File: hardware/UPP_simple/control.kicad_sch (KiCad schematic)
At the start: 9 parts, among them U1 STM32G0C1KCTxN

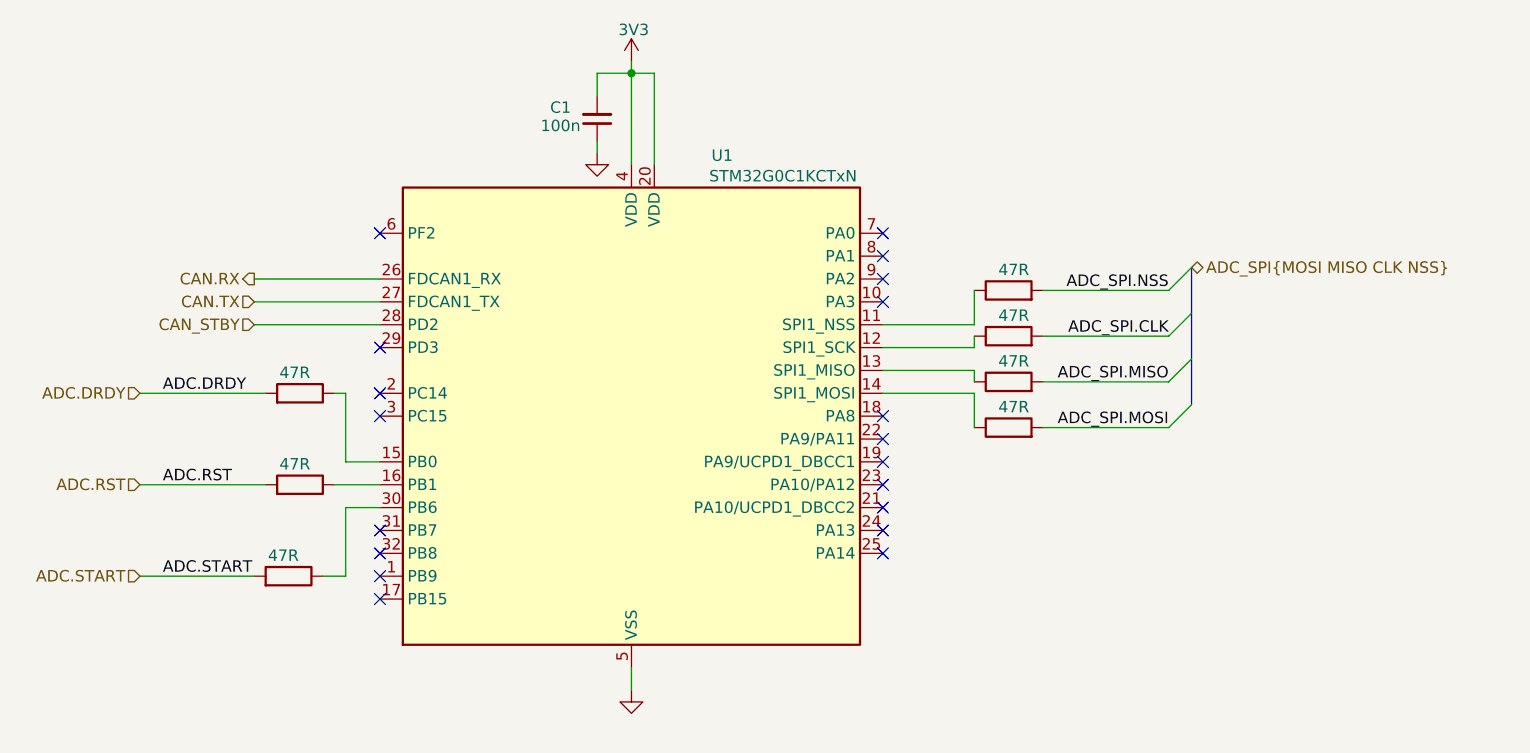
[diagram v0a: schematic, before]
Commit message: Changed Opamps cleared schematic
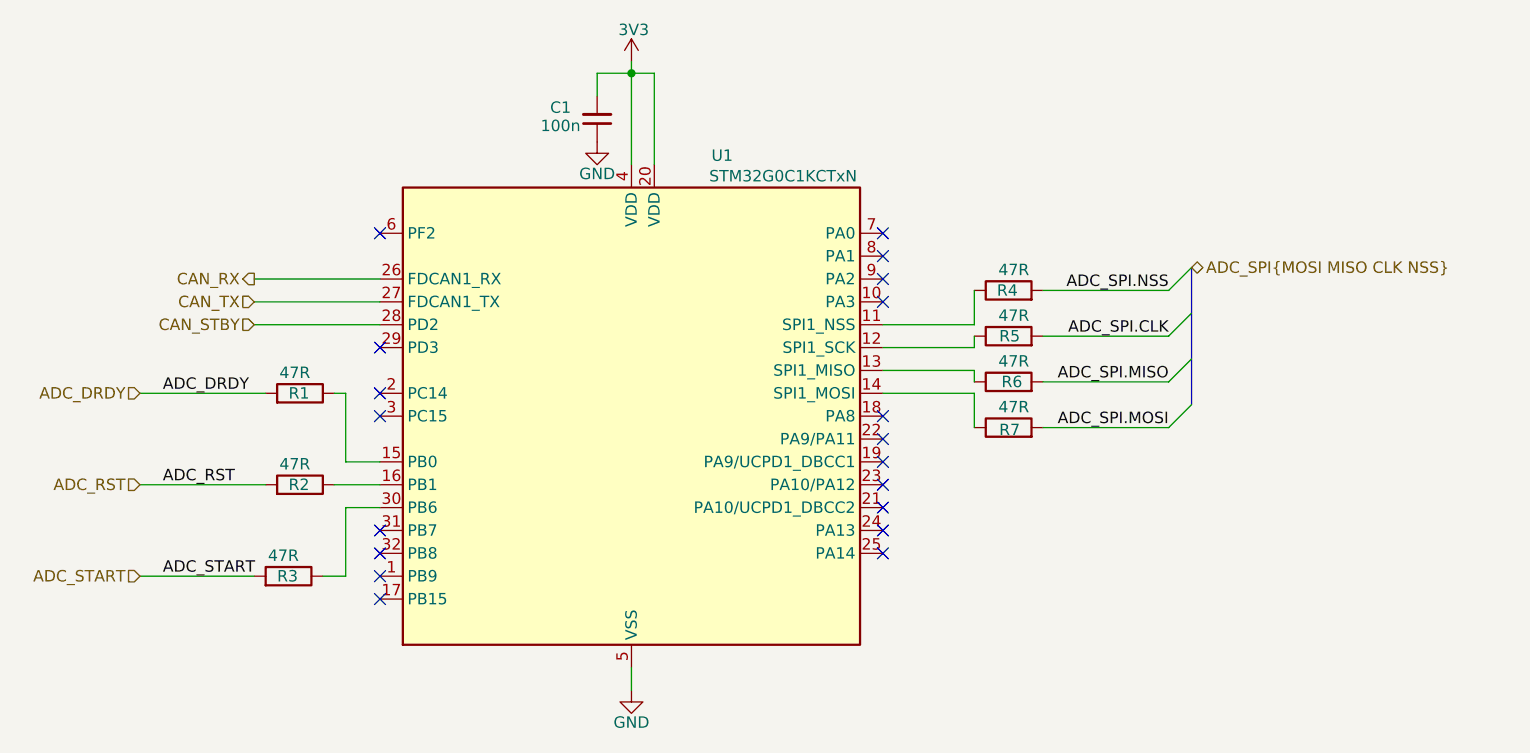
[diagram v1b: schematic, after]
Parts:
- renumbered R9 to R1, R15 to R2, R14 to R3, R13 to R4, R12 to R5, R11 to R6, R10 to R7
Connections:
- net ADC.DRDY renamed ADC_DRDY
- net ADC.RST renamed ADC_RST
- net ADC.START renamed ADC_START
- net CAN.RX renamed CAN_RX
- net CAN.TX renamed CAN_TX
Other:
- title: Universal use measuring PCB -> Universal Measurement Board
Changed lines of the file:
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@@
 	(paper "A4")
 	(title_block
-		(title "Universal use measuring PCB")
+		(title "Universal Measurement Board")
 		(company "Author: Kacper Pawlak")
 	)
@@
 		(pts
 			(xy 171.45 90.17) (xy 161.29 90.17)
-		)
-		(stroke
-			(width 0)
-			(type default)
-		)
-	)
-	(wire
-		(pts
-			(xy 129.54 62.23) (xy 129.54 63.5)
 		)
 		(stroke
@@
 		)
 	)
-	(label "ADC.RST"
+	(label "ADC_RST"
 		(at 81.28 100.33 0)
 		(effects
@@
 		)
 	)
-	(label "ADC.DRDY"
+	(label "ADC_DRDY"
 		(at 81.28 90.17 0)
 		(effects
@@
 		)
 	)
-	(label "ADC.START"
+	(label "ADC_START"
 		(at 81.28 110.49 0)
 		(effects
@@
 		)
 	)
-	(hierarchical_label "ADC.RST"
+	(hierarchical_label "ADC_RST"
 		(shape input)
 		(at 78.74 100.33 180)
@@
 		)
 	)
-	(hierarchical_label "CAN.TX"
+	(hierarchical_label "CAN_TX"
 		(shape input)
 		(at 91.44 80.01 180)
@@
 		)
 	)
-	(hierarchical_label "ADC.DRDY"
+	(hierarchical_label "ADC_DRDY"
 		(shape input)
 		(at 78.74 90.17 180)
@@
 		)
 	)
-	(hierarchical_label "CAN.RX"
+	(hierarchical_label "CAN_RX"
 		(shape output)
 		(at 91.44 77.47 180)
@@
 		)
 	)
-	(hierarchical_label "ADC.START"
+	(hierarchical_label "ADC_START"
 		(shape input)
 		(at 78.74 110.49 180)
@@
 		(on_board yes)
 		(dnp no)
-		(fields_autoplaced yes)
 		(property "Reference" "#PWR03"
 			(at 133.35 129.54 0)
@@
 		)
 		(property "Value" "GND"
-			(at 133.35 128.27 0)
-			(effects
-				(font
-					(size 1.27 1.27)
-				)
-				(hide yes)
+			(at 133.35 126.746 0)
+			(effects
+				(font
+					(size 1.27 1.27)
+				)
 			)
 		)
@@
 		(on_board yes)
 		(dnp no)
-		(property "Reference" "R14"
-			(at 96.5201 107.95 90)
-			(effects
-				(font
-					(size 1.27 1.27)
-				)
-				(justify left)
-				(hide yes)
+		(property "Reference" "R3"
+			(at 93.98 110.49 90)
+			(effects
+				(font
+					(size 1.27 1.27)
+				)
+				(justify left)
 			)
 		)
@@
 			(project "UPP_simple"
 				(path "/b652b05a-4e3d-4ad1-b032-18886abe7d45/e37d7555-464e-4542-8460-133370bc5076"
-					(reference "R14")
-					(unit 1)
-				)
-			)
-		)
-	)
-	(symbol
-		(lib_id "power:GND")
-		(at 129.54 63.5 0)
-		(unit 1)
-		(exclude_from_sim no)
-		(in_bom yes)
-		(on_board yes)
-		(dnp no)
-		(fields_autoplaced yes)
-		(property "Reference" "#PWR067"
-			(at 129.54 69.85 0)
-			(effects
-				(font
-					(size 1.27 1.27)
-				)
-				(hide yes)
-			)
-		)
-		(property "Value" "GND"
-			(at 129.54 68.58 0)
-			(effects
-				(font
-					(size 1.27 1.27)
-				)
-				(hide yes)
-			)
-		)
-		(property "Footprint" ""
-			(at 129.54 63.5 0)
-			(effects
-				(font
-					(size 1.27 1.27)
-				)
-				(hide yes)
-			)
-		)
-		(property "Datasheet" ""
-			(at 129.54 63.5 0)
-			(effects
-				(font
-					(size 1.27 1.27)
-				)
-				(hide yes)
-			)
-		)
-		(property "Description" "Power symbol creates a global label with name \"GND\" , ground"
-			(at 129.54 63.5 0)
-			(effects
-				(font
-					(size 1.27 1.27)
-				)
-				(hide yes)
-			)
-		)
-		(pin "1"
-		)
-		(instances
-			(project "UPP_simple"
-				(path "/b652b05a-4e3d-4ad1-b032-18886abe7d45/e37d7555-464e-4542-8460-133370bc5076"
-					(reference "#PWR067")
+					(reference "R3")
 					(unit 1)
 				)
@@
 		(on_board yes)
 		(dnp no)
-		(property "Reference" "R9"
-			(at 97.7901 87.63 90)
-			(effects
-				(font
-					(size 1.27 1.27)
-				)
-				(justify left)
-				(hide yes)
+		(property "Reference" "R1"
+			(at 95.25 90.17 90)
+			(effects
+				(font
+					(size 1.27 1.27)
+				)
+				(justify left)
 			)
 		)
@@
 			(project "UPP_simple"
 				(path "/b652b05a-4e3d-4ad1-b032-18886abe7d45/e37d7555-464e-4542-8460-133370bc5076"
-					(reference "R9")
+					(reference "R1")
 					(unit 1)
 				)
@@
 		(on_board yes)
 		(dnp no)
-		(property "Reference" "R15"
-			(at 97.7901 97.79 90)
-			(effects
-				(font
-					(size 1.27 1.27)
-				)
-				(justify left)
-				(hide yes)
+		(property "Reference" "R2"
+			(at 95.25 100.33 90)
+			(effects
+				(font
+					(size 1.27 1.27)
+				)
+				(justify left)
 			)
 		)
@@
 			(project "UPP_simple"
 				(path "/b652b05a-4e3d-4ad1-b032-18886abe7d45/e37d7555-464e-4542-8460-133370bc5076"
-					(reference "R15")
+					(reference "R2")
 					(unit 1)
 				)
@@
 		(on_board yes)
 		(dnp no)
-		(property "Reference" "R13"
-			(at 173.9899 76.2 90)
-			(effects
-				(font
-					(size 1.27 1.27)
-				)
-				(justify left)
-				(hide yes)
+		(property "Reference" "R4"
+			(at 176.276 78.74 90)
+			(effects
+				(font
+					(size 1.27 1.27)
+				)
+				(justify left)
 			)
 		)
@@
 			(project "UPP_simple"
 				(path "/b652b05a-4e3d-4ad1-b032-18886abe7d45/e37d7555-464e-4542-8460-133370bc5076"
-					(reference "R13")
+					(reference "R4")
 					(unit 1)
 				)
@@
 		(on_board yes)
 		(dnp no)
-		(property "Reference" "R11"
-			(at 173.9899 86.36 90)
-			(effects
-				(font
-					(size 1.27 1.27)
-				)
-				(justify left)
-				(hide yes)
+		(property "Reference" "R6"
+			(at 176.784 88.9 90)
+			(effects
+				(font
+					(size 1.27 1.27)
+				)
+				(justify left)
 			)
 		)
@@
 			(project "UPP_simple"
 				(path "/b652b05a-4e3d-4ad1-b032-18886abe7d45/e37d7555-464e-4542-8460-133370bc5076"
-					(reference "R11")
+					(reference "R6")
 					(unit 1)
 				)
@@
 	)
 	(symbol
+		(lib_id "power:GND")
+		(at 129.54 62.23 0)
+		(unit 1)
+		(exclude_from_sim no)
+		(in_bom yes)
+		(on_board yes)
+		(dnp no)
+		(property "Reference" "#PWR043"
+			(at 129.54 68.58 0)
+			(effects
+				(font
+					(size 1.27 1.27)
+				)
+				(hide yes)
+			)
+		)
+		(property "Value" "GND"
+			(at 129.54 65.786 0)
+			(effects
+				(font
+					(size 1.27 1.27)
+				)
+			)
+		)
+		(property "Footprint" ""
+			(at 129.54 62.23 0)
+			(effects
+				(font
+					(size 1.27 1.27)
+				)
+				(hide yes)
+			)
+		)
+		(property "Datasheet" ""
+			(at 129.54 62.23 0)
+			(effects
+				(font
+					(size 1.27 1.27)
+				)
+				(hide yes)
+			)
+		)
+		(property "Description" "Power symbol creates a global label with name \"GND\" , ground"
+			(at 129.54 62.23 0)
+			(effects
+				(font
+					(size 1.27 1.27)
+				)
+				(hide yes)
+			)
+		)
+		(pin "1"
+		)
+		(instances
+			(project "UMB"
+				(path "/b652b05a-4e3d-4ad1-b032-18886abe7d45/e37d7555-464e-4542-8460-133370bc5076"
+					(reference "#PWR043")
+					(unit 1)
+				)
+			)
+		)
+	)
+	(symbol
 		(lib_id "Device:R")
 		(at 175.26 93.98 90)
@@
 		(on_board yes)
 		(dnp no)
-		(property "Reference" "R10"
-			(at 173.9899 91.44 90)
-			(effects
-				(font
-					(size 1.27 1.27)
-				)
-				(justify left)
-				(hide yes)
+		(property "Reference" "R7"
+			(at 176.53 94.234 90)
+			(effects
+				(font
+					(size 1.27 1.27)
+				)
+				(justify left)
 			)
 		)
@@
 			(project "UPP_simple"
 				(path "/b652b05a-4e3d-4ad1-b032-18886abe7d45/e37d7555-464e-4542-8460-133370bc5076"
-					(reference "R10")
+					(reference "R7")
 					(unit 1)
 				)
@@
 		(on_board yes)
 		(dnp no)
-		(property "Reference" "R12"
-			(at 173.9899 81.28 90)
-			(effects
-				(font
-					(size 1.27 1.27)
-				)
-				(justify left)
-				(hide yes)
+		(property "Reference" "R5"
+			(at 176.53 83.82 90)
+			(effects
+				(font
+					(size 1.27 1.27)
+				)
+				(justify left)
 			)
 		)
@@
 			(project "UPP_simple"
 				(path "/b652b05a-4e3d-4ad1-b032-18886abe7d45/e37d7555-464e-4542-8460-133370bc5076"
-					(reference "R12")
+					(reference "R5")
 					(unit 1)
 				)
